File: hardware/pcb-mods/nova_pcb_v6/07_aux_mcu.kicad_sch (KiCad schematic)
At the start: 3 parts, among them J10 SSD1331_OLED, J11 WS2812B_Strip, U12 Arduino_Nano

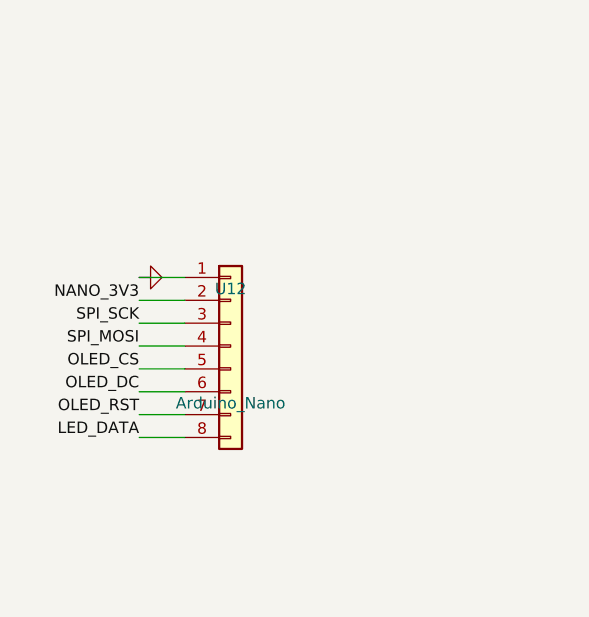
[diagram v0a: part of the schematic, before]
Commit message: pcb(v6-power-v2): fork to v2 — full reroute, safety chain, off-board INA226, DRC clean
- Fork nova_pcb_v6_power -> _v2 (v1 frozen); placement redone power-flow-first
- Safety chain board sync: Q3 e-stop inverter, Q4 EN_JET cutoff, R16, C8/C9
- INA226 modules converted off-board: footprints stripped to 4-pin I2C headers,
  RAW nets eliminated (bench wiring card in ROUTING_HANDOFF.md Step 8)
- All power routed 1.5/3.0mm per netclass, LEG pour L-shape, hip doubled F+B
- All signal nets routed headless via pre-commit collision checker:
  B.Cu lanes y137.5-139.9 + F.Cu verticals + via pairs; V5_AUX spine gap
  bridged x114.5; board min via relaxed to 0.45/0.25 (PCBWay standard)
- DRC: 0 errors, 0 unrouted; 2 zone-island seams left for GUI (Step 9)

Co-Authored-By: Claude Fable 5 <noreply@anthropic.com>
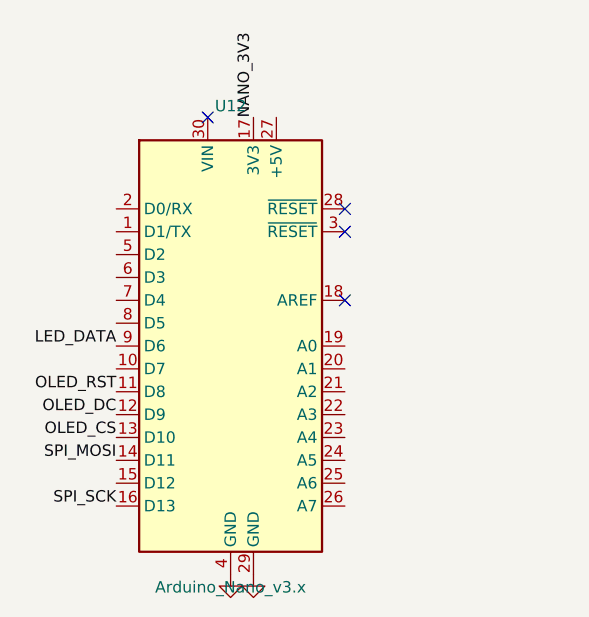
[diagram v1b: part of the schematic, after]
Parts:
- U12: value Arduino_Nano -> Arduino_Nano_v3.x; footprint Connector_PinHeader_2.54mm:PinHeader_1x08_P2.54mm_Vertical -> Module:Arduino_Nano; symbol Connector_Generic:Conn_01x08 -> MCU_Module:Arduino_Nano_v3.x
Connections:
- net GND: now also U12.29 (GND), U12.4 (GND); no longer U12.1 (Pin_1)
- net LED_DATA: now also U12.9 (D6); no longer U12.8 (Pin_8)
- net NANO_3V3: now also U12.17 (3V3); no longer U12.2 (Pin_2)
- net OLED_CS: now also U12.13 (D10); no longer U12.5 (Pin_5)
- net OLED_DC: now also U12.12 (D9); no longer U12.6 (Pin_6)
- net OLED_RST: now also U12.11 (D8); no longer U12.7 (Pin_7)
- net SPI_MOSI: now also U12.14 (D11); no longer U12.4 (Pin_4)
- net SPI_SCK: now also U12.16 (D13); no longer U12.3 (Pin_3)
- no-connect marks 0 -> 4
